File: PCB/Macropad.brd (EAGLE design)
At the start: 127 x 133.3 mm, 76 parts, among them IC1 LM2937, U1 EC11E09244AQ, X1 ZX62D-B-5PA8

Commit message: pcb updates
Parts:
- moved IC1 0.51 mm to (84.7, 116.4)
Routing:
- net GND: track 283.3 -> 289.3 mm
- net D+: track 46.6 -> 44.5 mm
- net +5V: track 60.5 -> 62.5 mm
- net ROW_2: track 122.6 -> 123.7 mm
- net +3V3: track 169.2 -> 168.2 mm

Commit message: Final touchups with TA
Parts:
- moved C3 27.3 mm to (104.3, 85.5), turned to 180 degrees
- moved U$2 2.95 mm to (108.6, 105.0)
- moved C11 2.90 mm to (103.6, 108.4)
- moved C12 2.85 mm to (107.5, 108.4)
- turned C17 to 180 degrees
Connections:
- net D+: now also JP1.3; no longer JP1.2
- net D-: now also JP1.2; no longer JP1.3
- net GND: now also X1.S1, X1.S2, X1.S3, X1.S4
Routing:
- net GND: track 289.3 -> 311.8 mm, vias 6 -> 7
- net PF0: track 75.6 -> 84.2 mm
- net PF1: track 70.2 -> 78.4 mm
- net PF2: track 92.7 -> 100.6 mm
- net D-: track 48.4 -> 41.6 mm, vias 0 -> 1
- net OSC1: track 11.2 -> 8.27 mm
- net OSC0: track 11.3 -> 8.44 mm
- net +3V3: track 168.2 -> 170.4 mm, vias 0 -> 1
- net ST7735_CARD_CS: track 26.9 -> 28.2 mm
- net RESET: track 36.1 -> 37.3 mm
- net D+: track 44.5 -> 43.9 mm, vias 2 -> 1
- net VDDC: vias 3 -> 2

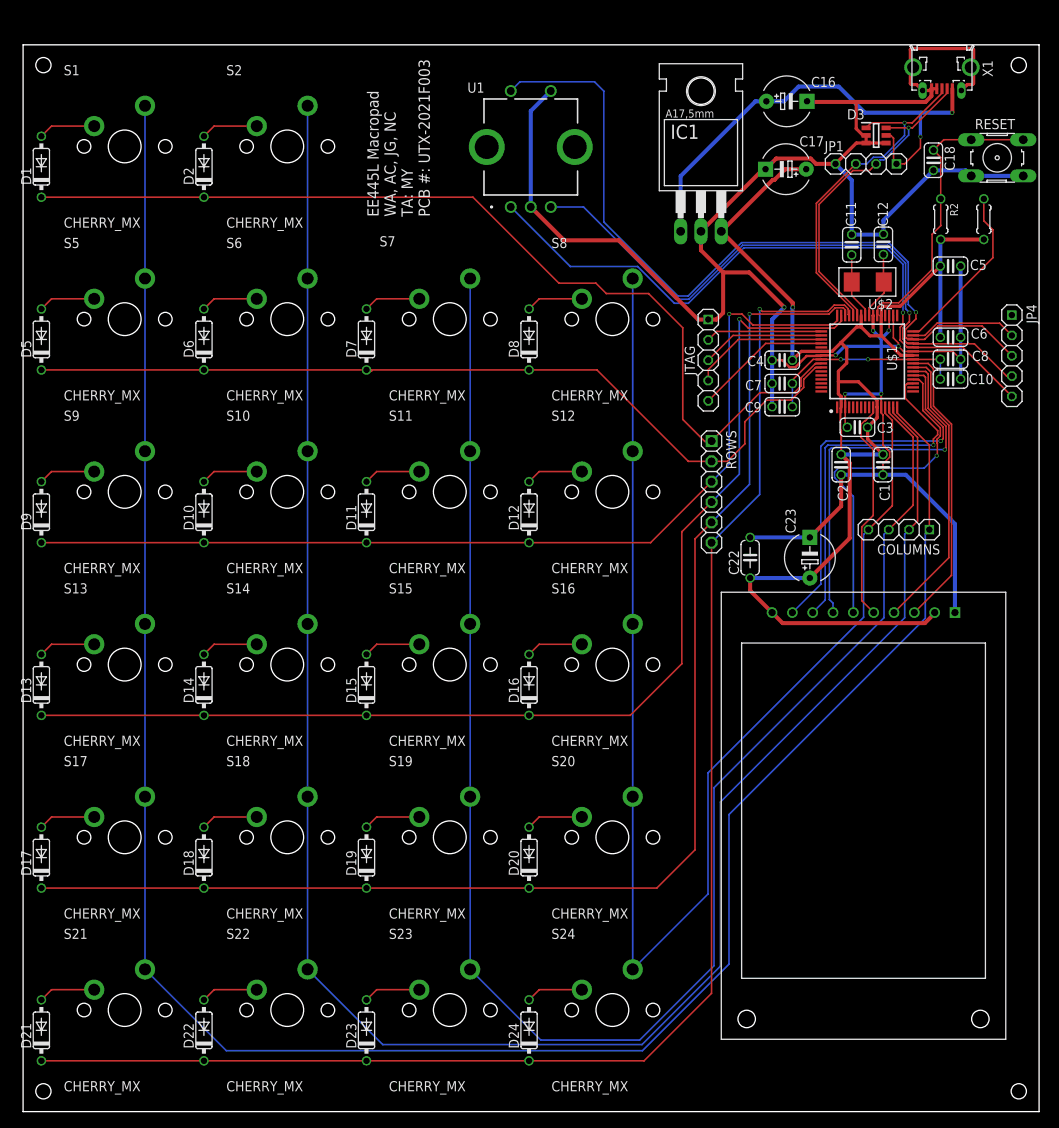
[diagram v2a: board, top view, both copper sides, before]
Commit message: Reduced board to 4.98x5 inches
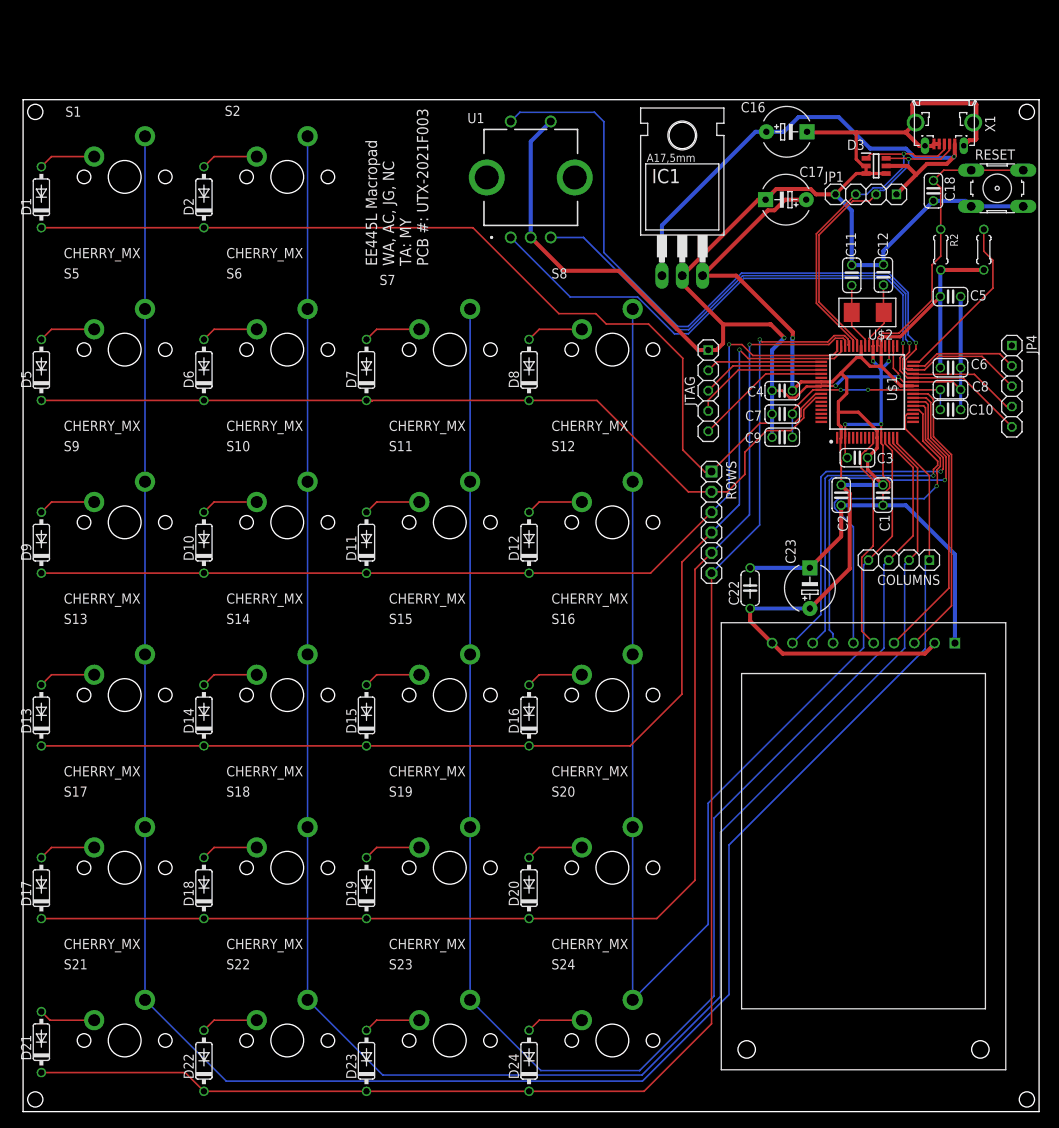
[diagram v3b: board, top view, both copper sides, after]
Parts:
- moved X1 6.92 mm to (115.2, 125.8)
- moved IC1 6.01 mm to (82.4, 110.8)
- moved C1 3.81 mm to (107.5, 77.1)
- moved C12 3.81 mm to (107.5, 104.6)
- moved C17 3.81 mm to (95.4, 114.0)
- moved C18 3.81 mm to (113.8, 115.1)
- moved C2 3.81 mm to (102.3, 77.1)
- moved C3 3.81 mm to (104.3, 81.7)
- moved C5 3.81 mm to (115.9, 101.9)
- moved C6 3.81 mm to (115.9, 93.0)
- moved C7 3.81 mm to (94.9, 87.2)
- moved C8 3.81 mm to (115.9, 90.2)
- moved C9 3.81 mm to (94.9, 84.3)
- moved COLUMNS 3.81 mm to (109.5, 68.9)
- moved D1 3.81 mm to (2.29, 114.3)
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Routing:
- net +3V3: track 170.4 -> 175.2 mm
- net +5V: track 62.5 -> 65.6 mm, vias 2 -> 1
- net GND: track 311.8 -> 309.8 mm
- net ROW_5: track 187.9 -> 188.9 mm
- net D-: track 41.6 -> 40.7 mm
- net D+: track 43.9 -> 43.1 mm
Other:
- board size 127 x 133.3 mm -> 127 x 126.5 mm

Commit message: Evenly spaced the keys
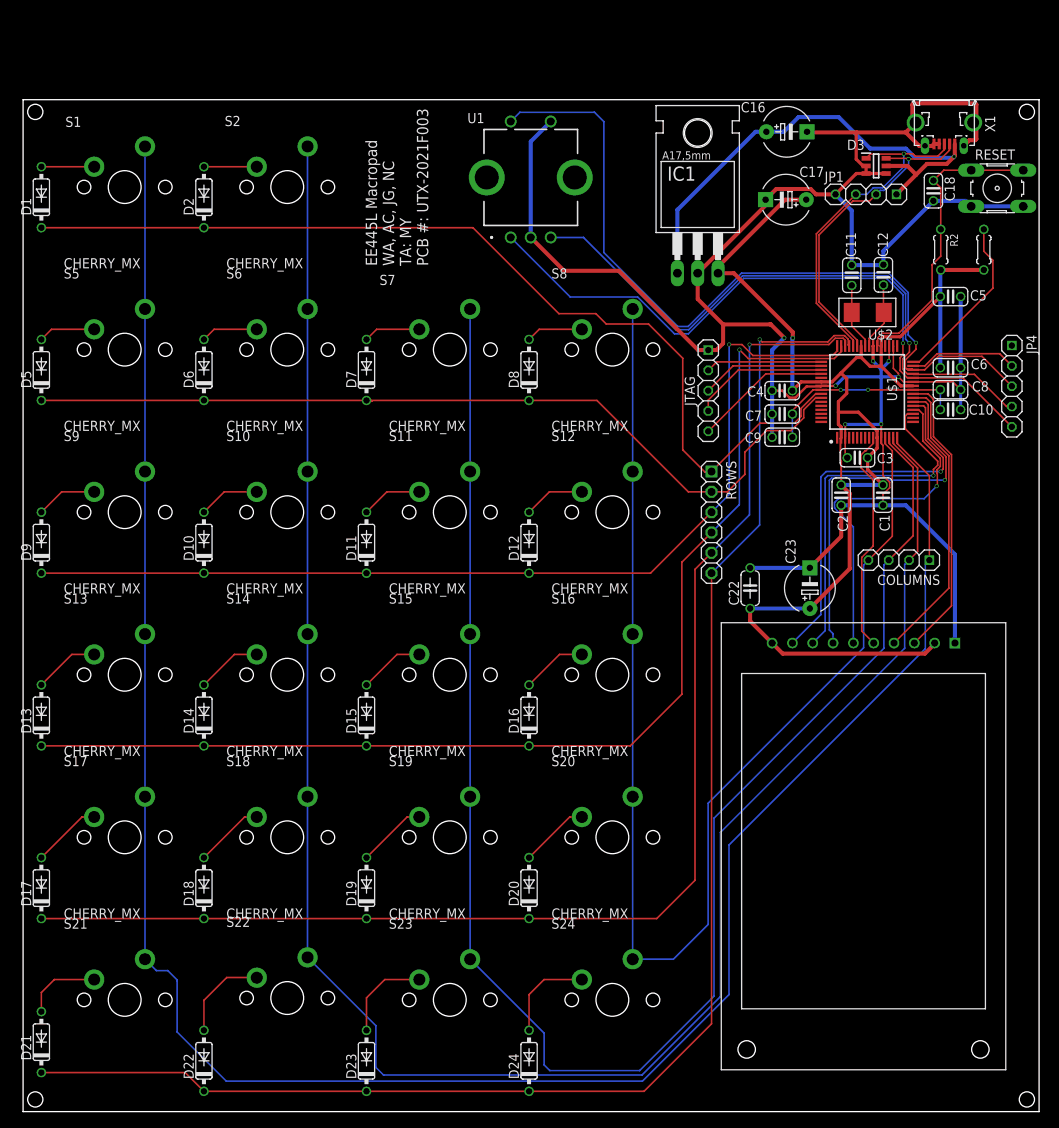
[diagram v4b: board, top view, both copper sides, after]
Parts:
- moved S22 5.31 mm to (33.0, 14.2)
- moved S21 5.08 mm to (12.7, 14.0)
- moved S23 5.08 mm to (53.3, 14.0)
- moved S24 5.08 mm to (73.7, 14.0)
- moved S17 3.81 mm to (12.7, 34.3)
- moved S18 3.81 mm to (33.0, 34.3)
- moved S19 3.81 mm to (53.3, 34.3)
- moved S20 3.81 mm to (73.7, 34.3)
- moved S13 2.54 mm to (12.7, 54.6)
- moved S14 2.54 mm to (33.0, 54.6)
- moved S15 2.54 mm to (53.3, 54.6)
- moved S16 2.54 mm to (73.7, 54.6)
- moved IC1 1.95 mm to (84.3, 111.2)
- moved S1 1.27 mm to (12.7, 115.6)
- moved S10 1.27 mm to (33.0, 74.9)
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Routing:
- net COLUMN_3: track 170.4 -> 163.2 mm
- net N$30: track 7.13 -> 11.9 mm
- net N$29: track 7.13 -> 11.6 mm
- net N$28: track 7.13 -> 11.6 mm
- net +3V3: track 175.2 -> 171.8 mm
- net N$27: track 7.05 -> 9.66 mm
- net GND: track 309.8 -> 307.7 mm
- net N$26: track 7.13 -> 8.71 mm
- net N$23: track 7.13 -> 8.71 mm
- net N$24: track 7.13 -> 8.71 mm
- net N$25: track 7.13 -> 8.71 mm
- net COLUMN_1: track 248.8 -> 247.5 mm
- net +5V: track 65.6 -> 64.5 mm
- net N$22: track 7.13 -> 8.18 mm
- net N$21: track 7.13 -> 8.18 mm
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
